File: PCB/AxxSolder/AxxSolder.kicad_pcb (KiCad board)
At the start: 2 copper layers, 39 x 71 mm, 82 parts, among them IC1 LTC4440AHMS8E-5#PBF, IC2 STM32G431KBT6, IC3 TMP236AQDBZRQ1, IC4 OPA2333AIDRBR, IC5 STM32G431KBT6, J1 Conn_01x07_Male, J4 Conn_01x07_Male, Q2 2N7002NXAKR, U1 PEC11L-4220F-S0015, U2 BSC014N04LS

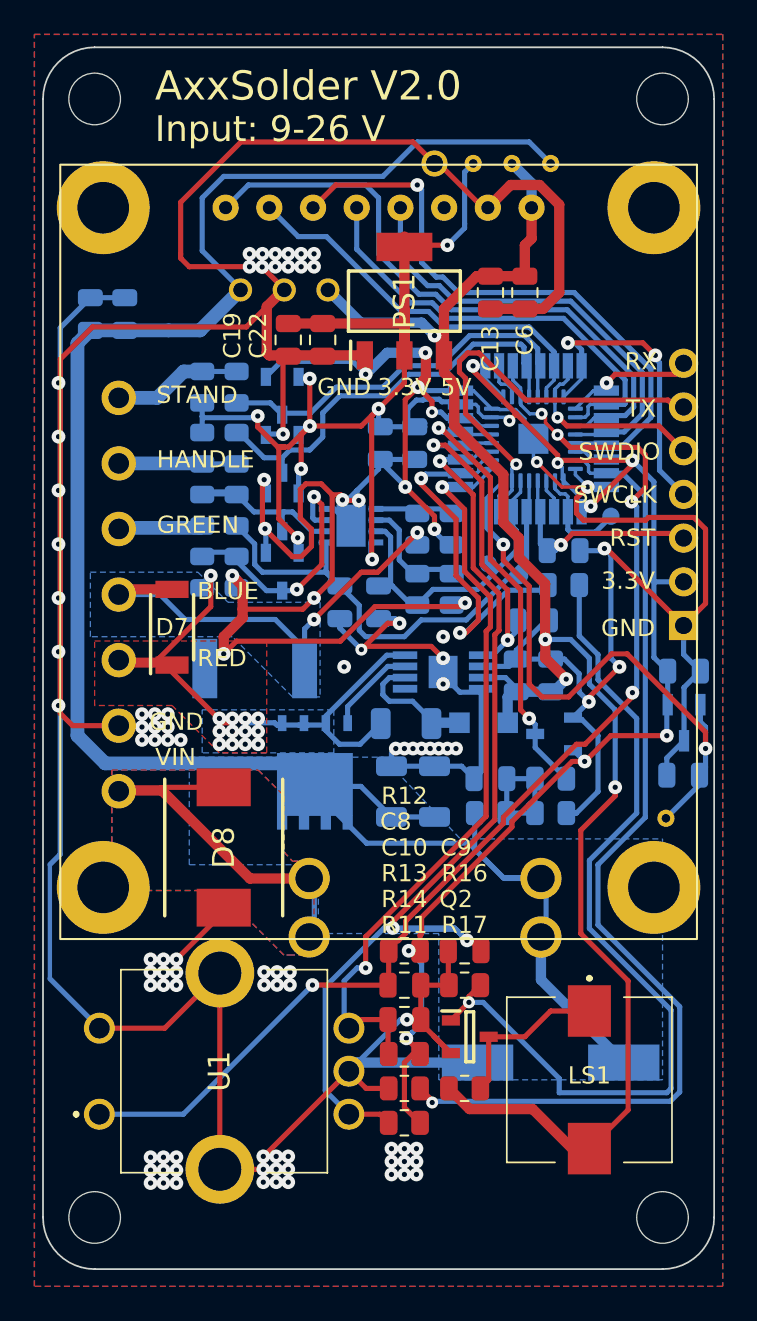
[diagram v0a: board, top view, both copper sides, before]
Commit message: Change to new, more cost effective VCC->5V DC/DC solution, update to AxxSolder V2.1
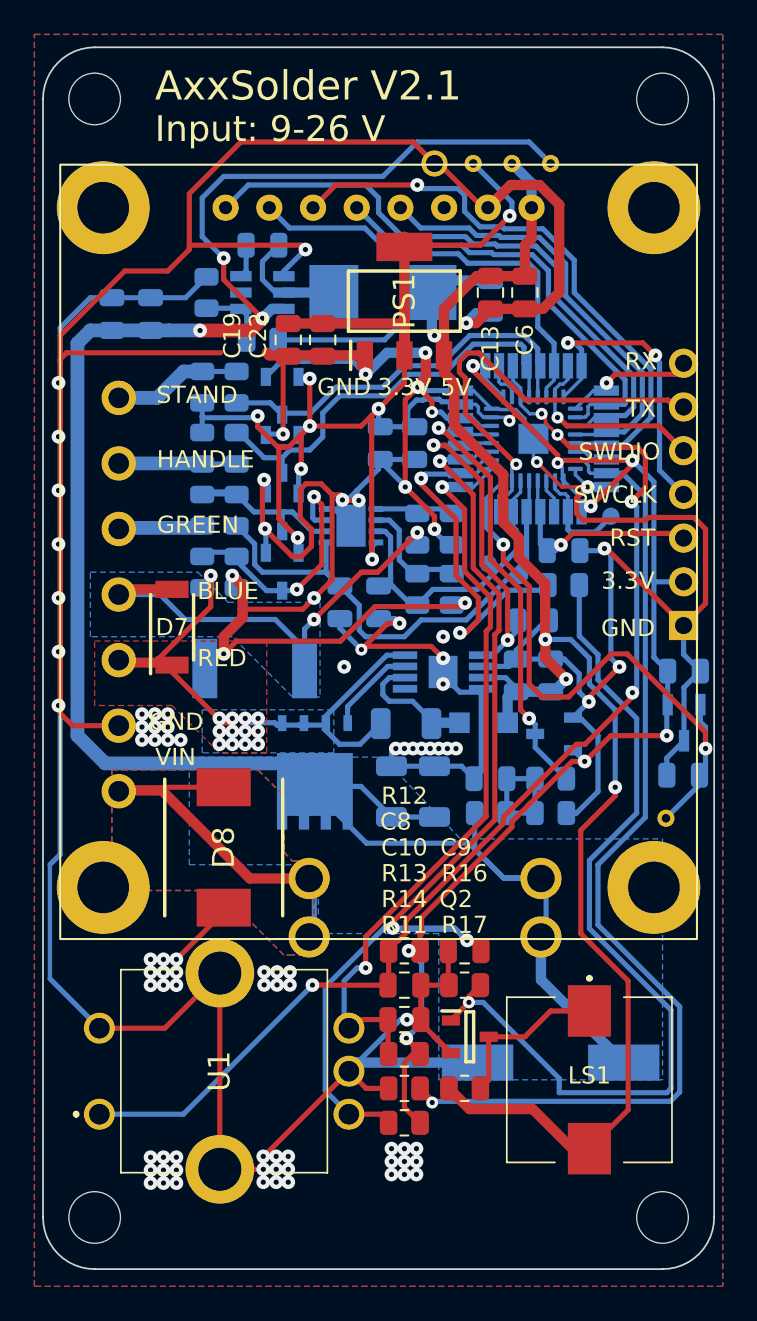
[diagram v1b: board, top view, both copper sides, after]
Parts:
- removed PS2: TSR_2-2450, TSR_2-2450:TSR-2
- added C24: 10u, Capacitor_SMD:C_0805_2012Metric, B.Cu at (109.8, 58.5)
- added C25: 10u, Capacitor_SMD:C_0805_2012Metric, B.Cu at (123.0, 61.5)
- added IC6: TPS54302DDCR, TPS54302DDCR:SOT95P280X110-6N, B.Cu at (109.8, 61.2)
- added L1: SRP7028CC-100M, SRP7028CC-100M:INDPM7366X300N, B.Cu at (116.8, 61.2)
- added R27: 4k7, Resistor_SMD:R_0805_2012Metric, B.Cu at (109.8, 64.0)
- added R28: 4k7, Resistor_SMD:R_0805_2012Metric, B.Cu at (106.5, 61.2)
- TP1: value TestPoint -> AmbTemp_TP
- TP3: value TestPoint -> GND_TP
- TP5: value TestPoint -> Thermocouple_TP
- TP6: value TestPoint -> Current_TP
- TP7: value TestPoint -> 5V_TP
- TP8: value TestPoint -> VDD_TP
- TP9: value TestPoint -> 3.3V_TP
- moved C21 3.50 mm to (103.2, 62.5)
- moved C14 0.75 mm to (101.0, 62.5)
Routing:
- net GND: track 408.8 -> 420.5 mm, vias 106 -> 96
- net +5V: track 97.8 -> 106.8 mm
- net Net-(IC6-SW): track 0.00 -> 6.85 mm
- net VDD: track 121.1 -> 125.2 mm, vias 0 -> 3
- net Net-(IC6-FB): track 0.00 -> 3.96 mm
- net +3.3V: track 156.3 -> 159.4 mm
- net /SPI_DC: track 22.8 -> 25.0 mm
- net Net-(IC6-BOOT): track 0.00 -> 1.92 mm
- net /SPI_CS: track 35.0 -> 34.2 mm
- net /SPI_MOSI: track 26.5 -> 25.9 mm
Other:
- board text added: "AxxSolder V2.1"
- board text removed: "AxxSolder V2.0"

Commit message: Clean and structure PCB Layout and update to AxxSolder V2.1
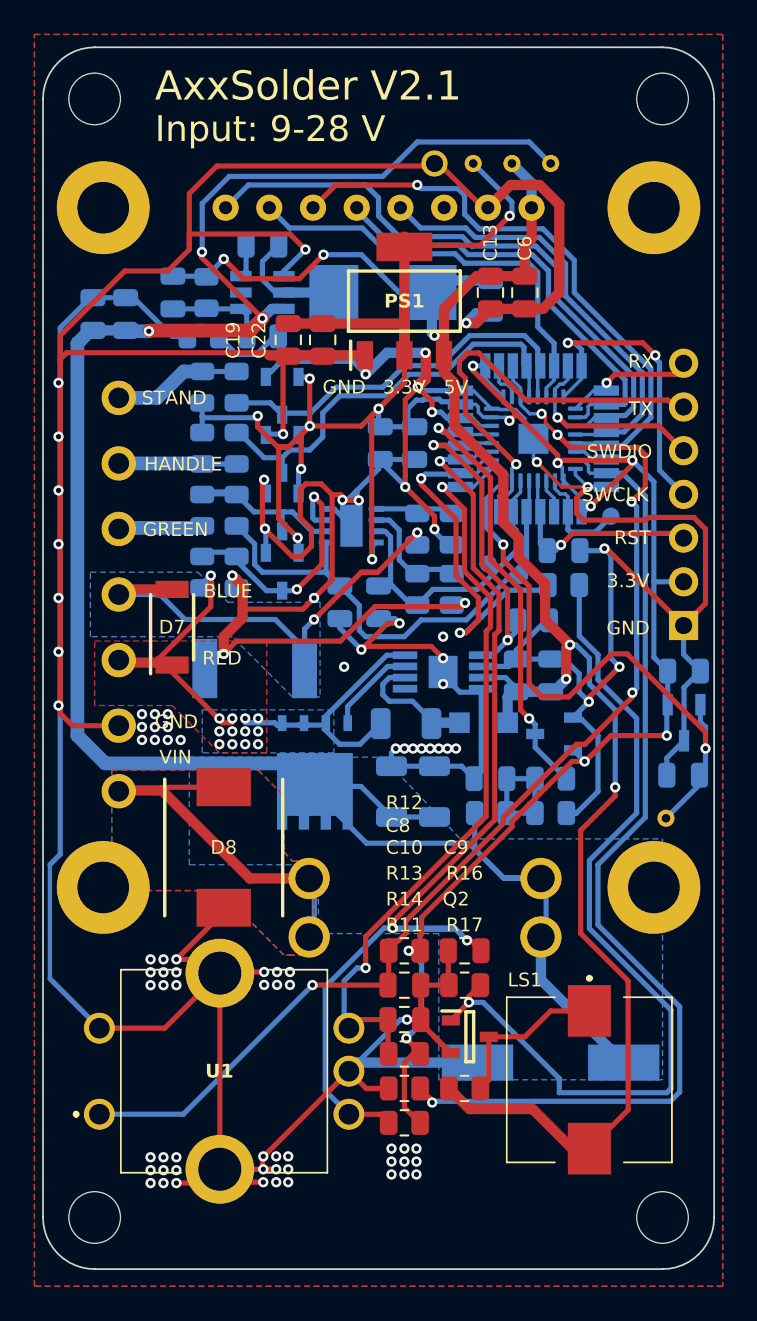
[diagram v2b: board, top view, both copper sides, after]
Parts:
- added C26: 75p, Capacitor_SMD:C_0805_2012Metric, B.Cu at (104.5, 61.2)
- added R29: 13k3, Resistor_SMD:R_0805_2012Metric, B.Cu at (106.3, 63.8)
- C25: value 10u -> 22u
- R27: value 4k7 -> 100k
- R28: value 4k7 -> 49.9
- moved C21 1.45 mm to (101.8, 62.5)
- moved C14 1.10 mm to (99.9, 62.5)
- moved R27 0.20 mm to (109.8, 63.8)
- turned C13 to 90 degrees
- turned C6 to 90 degrees
- turned L1 to 0 degrees
- turned R12 to 180 degrees
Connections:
- net /AMBIENT_TEMP renamed /Ambient_temp
- net /BUZZER renamed /Buzzer
- C13 pad 1: +5V -> GND
- C13 pad 2: GND -> +5V
- C23 pad 1: (no net) -> VDD
- C23 pad 2: (no net) -> GND
- C6 pad 1: +5V -> GND
- C6 pad 2: GND -> +5V
- L1 pad 1: +5V -> Net-(IC6-SW)
- L1 pad 2: Net-(IC6-SW) -> +5V
- R12 pad 1: /ENC_Button -> +3.3V
- R12 pad 2: +3.3V -> /ENC_Button
- R27 pad 2: +5V -> Net-(R27-Pad2)
- R28 pad 1: GND -> +5V
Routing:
- net GND: track 420.5 -> 432.8 mm
- net +5V: track 106.8 -> 112.8 mm, vias 4 -> 6
- net Net-(R27-Pad2): track 0.00 -> 4.37 mm
- net Net-(IC6-FB): track 3.96 -> 5.97 mm
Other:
- board text added: "CLK"
- board text added: "DIO"
- board text added: "Input: 9-28 V"
- board text removed: "Input: 9-26 V"

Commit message: Change silkscreen to Input: 9-24V and optimize board layout
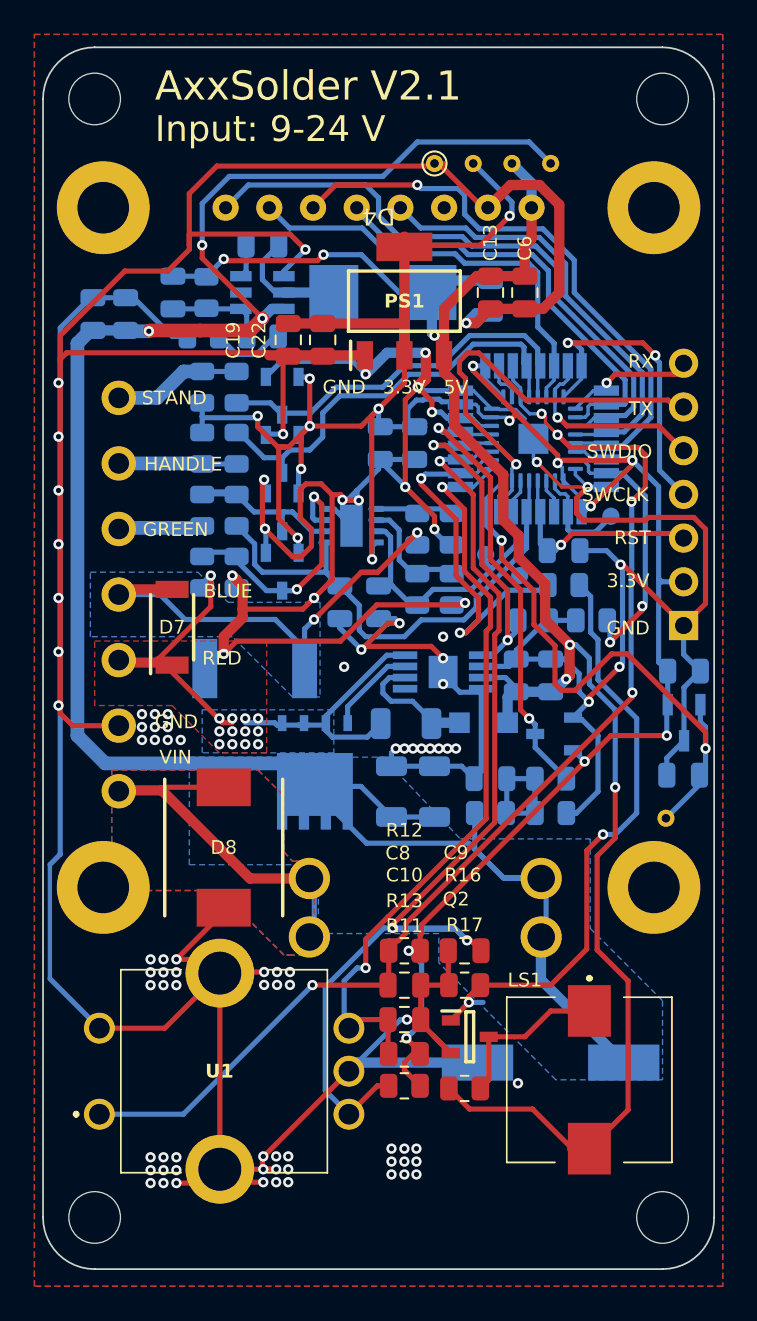
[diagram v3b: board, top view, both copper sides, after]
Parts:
- R14: moved to B.Cu
- TP3: footprint testpin black 1mm:testpin black 1mm -> TestPoint:TestPoint_THTPad_D1.0mm_Drill0.5mm
- moved R14 29.3 mm to (128.9, 80.3)
- moved R11 2.15 mm to (118.0, 107.3)
- moved TP6 0.56 mm to (122.7, 76.5)
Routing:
- net Net-(IC2-PB8-BOOT0): track 58.8 -> 15.8 mm, vias 1 -> 2
- net Net-(Q2-Pad1): track 51.0 -> 34.8 mm, vias 1 -> 2
- net +3.3V: track 159.4 -> 156.6 mm
- net GND: track 432.8 -> 430.3 mm, vias 96 -> 97
- net +5V: track 112.8 -> 111.2 mm
- net /Ambient_temp: track 35.4 -> 34.2 mm
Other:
- board text added: "Input: 9-24 V"
- board text removed: "Input: 9-28 V"

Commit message: Fix output voltage from DC/DC by switching values of R28 and R27. Also change value of C24
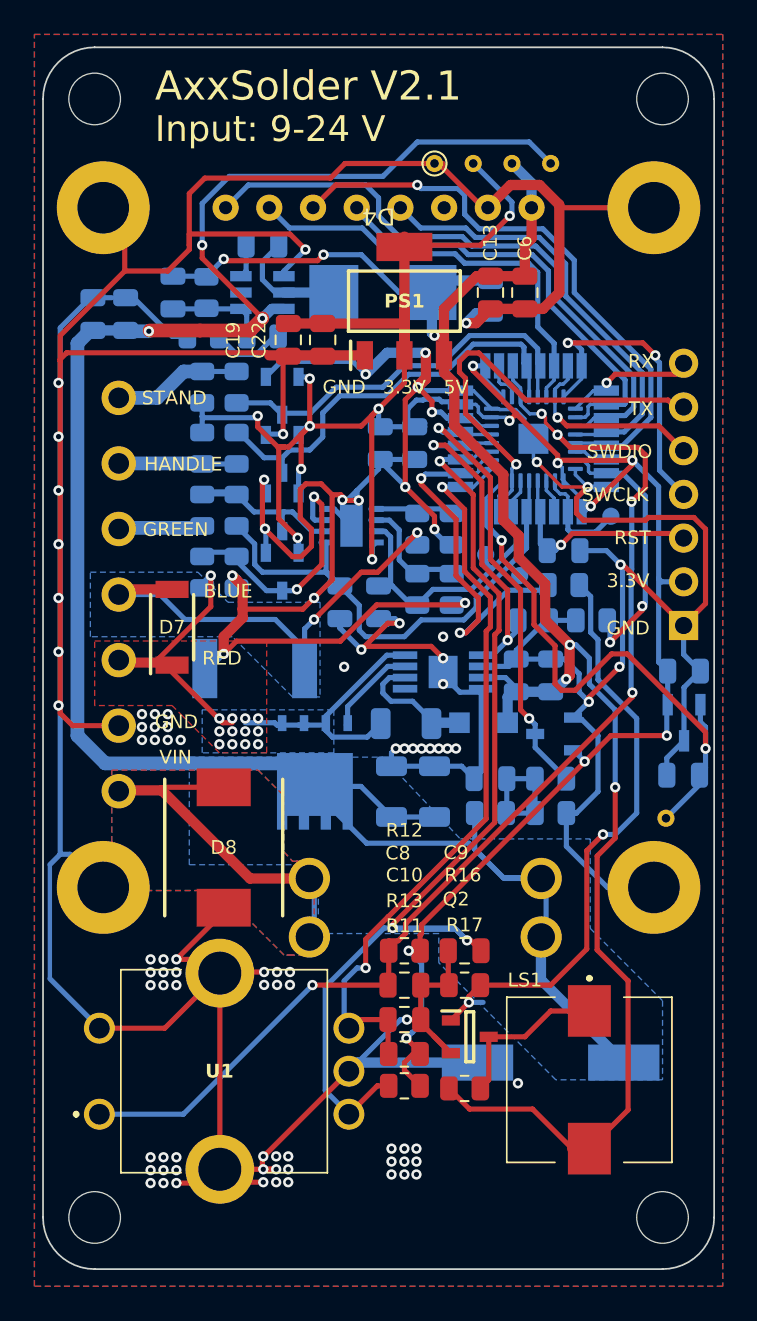
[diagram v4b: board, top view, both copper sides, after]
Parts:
- C24: value 10u -> 100n
- R27: value 100k -> 49,9
- R28: value 49.9 -> 100k
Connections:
- net /HandleStand renamed /Stand_sense
- net /Input0 renamed /Handle_inp
- net /Input1 renamed /Stand_inp
- net /RST renamed /NRST
- net /TipChanger renamed /Handle_sense
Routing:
- net GND: track 430.3 -> 452.8 mm
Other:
- board text added: "NRST"

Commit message: Improve PCB layout slightly and update gerbers with cu-filled GND layer
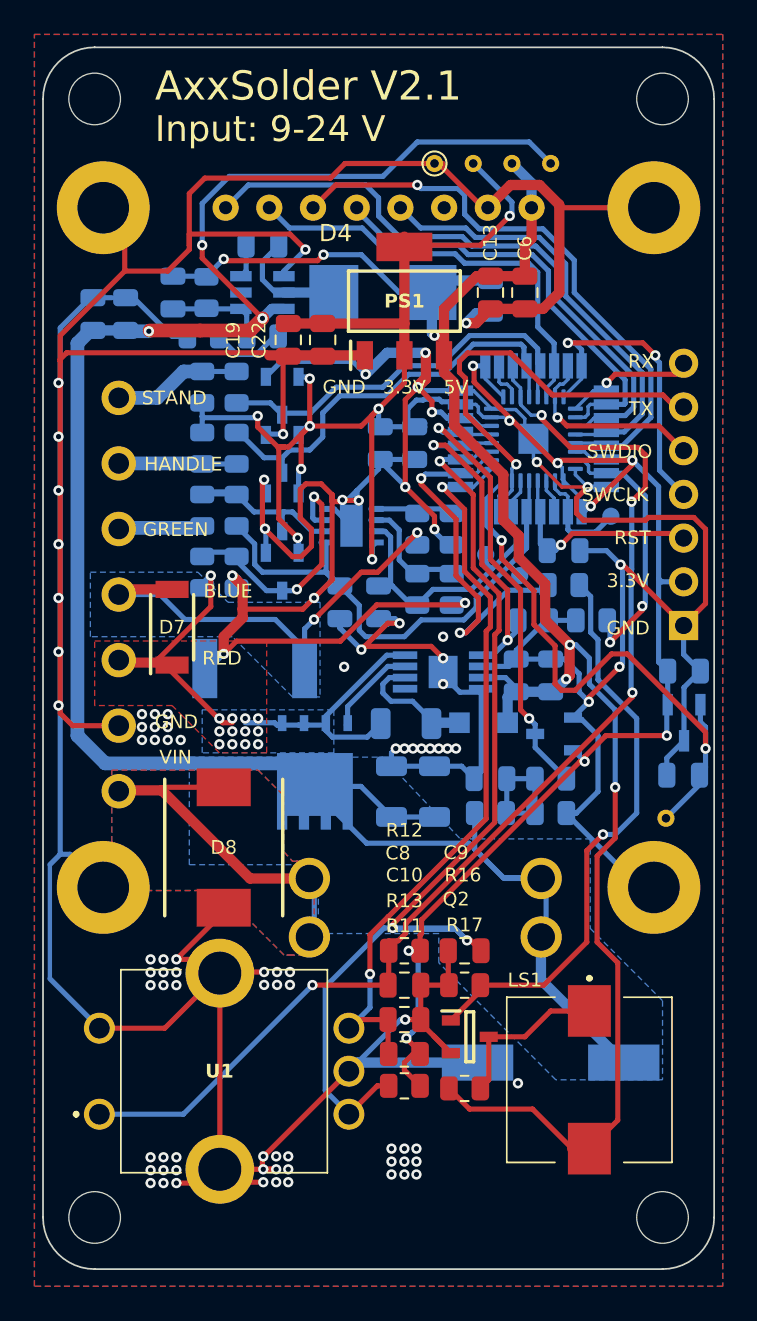
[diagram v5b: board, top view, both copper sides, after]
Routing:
- net +3.3V: track 156.6 -> 153.7 mm
- net Net-(Q2-Pad1): track 34.8 -> 33.7 mm, vias 2 -> 1
- net GND: track 452.8 -> 451.9 mm
- net /ENC_A: track 44.3 -> 43.8 mm
- net /ENC_Button: track 68.4 -> 68.3 mm, vias 5 -> 4

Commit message: Update PCB design to V2.2 - correct fault in 5V DC/DC and change the VDD tVS diode to a 600W instead of 1.5kW and small PCB improvements
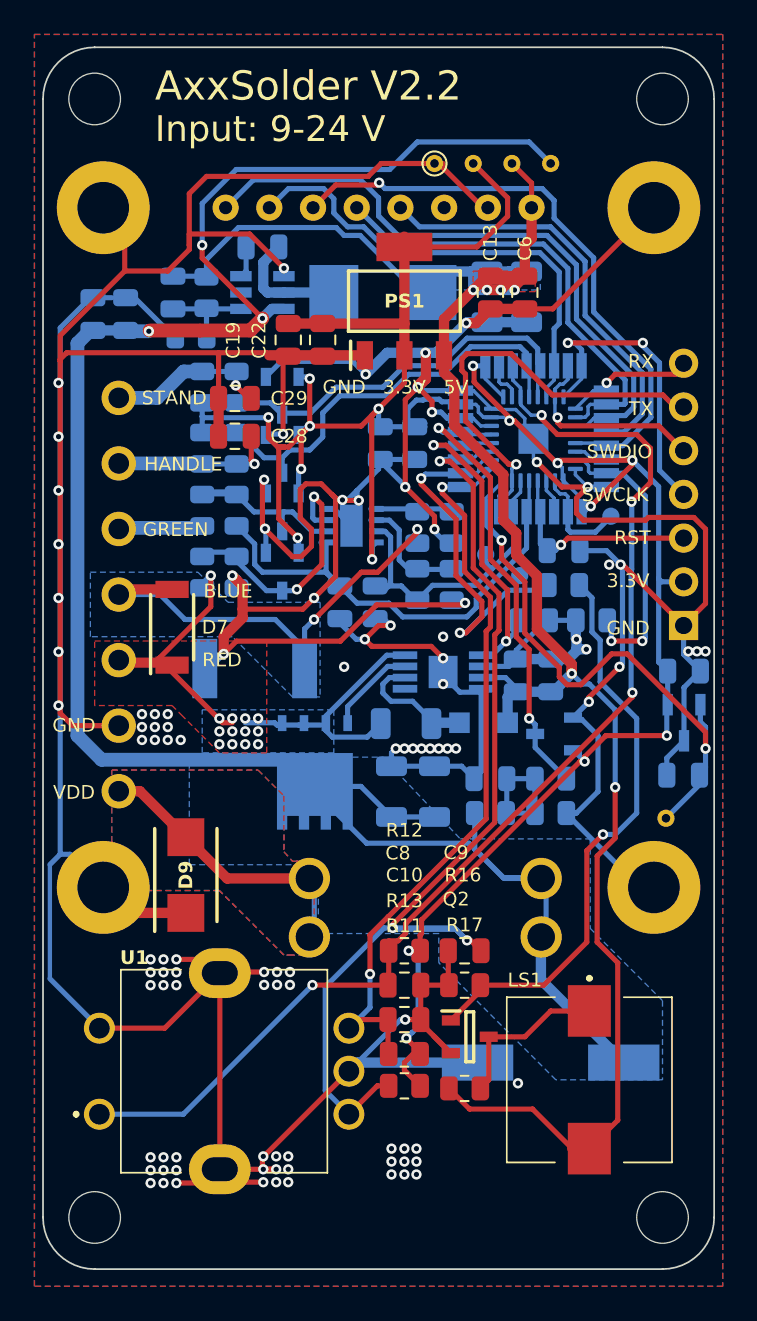
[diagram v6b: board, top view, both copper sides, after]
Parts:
- removed D8: SMCJ24CA, SMCJ24CA:DIONM7969X262N
- removed R27: 49,9, Resistor_SMD:R_0805_2012Metric
- added C27: 22u, Capacitor_SMD:C_1206_3216Metric, B.Cu at (125.1, 61.5)
- added C28: 100n, Capacitor_SMD:C_0805_2012Metric, F.Cu at (108.2, 69.6)
- added C29: 100n, Capacitor_SMD:C_0805_2012Metric, F.Cu at (108.2, 67.4)
- added D9: SMBJ24CA, SMBJ24CA:DIOM5436X261N, F.Cu at (105.3, 95.1)
- C17, C18: value 22u -> 22u/35V
- C25: footprint Capacitor_SMD:C_0805_2012Metric -> Capacitor_SMD:C_1206_3216Metric
- moved R29 0.70 mm to (105.6, 63.8)
- moved R24 0.29 mm to (118.8, 78.2)
- moved R26 0.29 mm to (120.8, 78.2)
- moved C16 0.20 mm to (116.3, 79.2)
- moved C25 0.20 mm to (122.8, 61.5)
- moved C24 0.10 mm to (109.8, 58.6)
- moved R23 0.10 mm to (120.8, 74.9)
- moved R25 0.10 mm to (118.8, 74.9)
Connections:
- R29 pad 1: Net-(R27-Pad2) -> Net-(IC6-FB)
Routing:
- net +5V: track 110.7 -> 119.2 mm
- net Net-(R27-Pad2): track 4.32 -> 0.00 mm
- net Net-(J1-Pin_7): track 20.6 -> 16.7 mm
- net /Handle_sense: track 6.93 -> 9.66 mm, vias 0 -> 1
- net /SPI_DC: track 25.0 -> 27.4 mm
- net VDD: track 124.9 -> 122.6 mm
- net /Stand_sense: track 7.48 -> 9.53 mm, vias 0 -> 1
- net /Thermocouple: track 32.6 -> 30.8 mm
- net /SPI_RST: track 36.2 -> 37.2 mm
- net Net-(IC2-PB8-BOOT0): track 15.8 -> 16.7 mm
- net /SPI_CS: track 34.3 -> 35.1 mm
- net /SPI_MOSI: track 25.9 -> 26.6 mm
- net /SPI_SCK: track 25.8 -> 26.4 mm
- net /ENC_Button: track 68.3 -> 69.0 mm
- net /Ambient_temp: track 34.2 -> 33.6 mm
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- added copper zone on B.Cu, net +5V
- added copper zone on F.Cu, net +5V
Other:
- board text added: "AxxSolder V2.2"
- board text added: "VDD+"
- board text removed: "AxxSolder V2.1"
- board text removed: "VIN"
